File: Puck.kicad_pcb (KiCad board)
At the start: 2 copper layers, 40.1 x 33 mm, 15 parts, among them J1 TYPE-C-31-M-12, J2 AUTO_PROG_UART, U1 ESP32-C6-MINI-1-H4, U2 MCP9808T-E_MS, U4 AP2112K-3.3TRG1

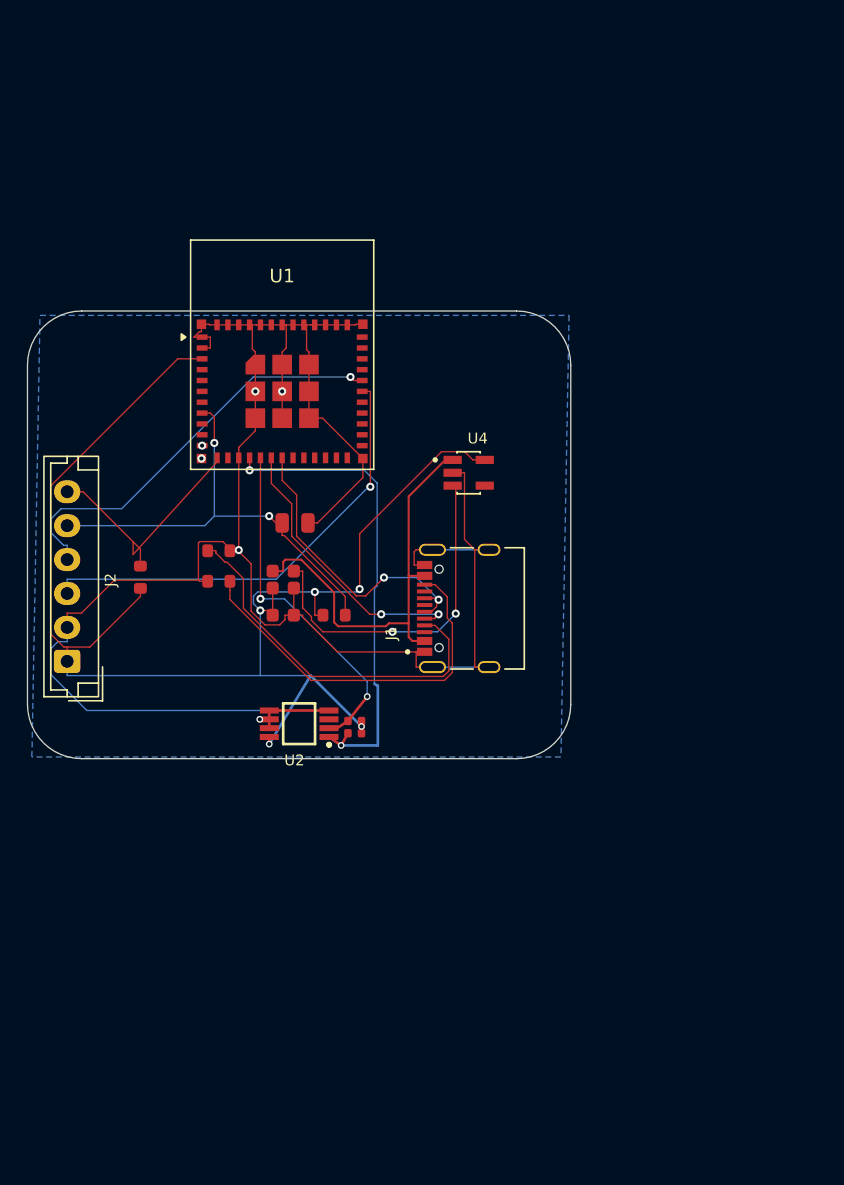
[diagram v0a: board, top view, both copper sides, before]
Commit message: Finished schematic + redid pcb layout
Original-author: Zachariah K. Sharma <zachariah.sharma@gmail.com>
Source-commit: d32a3a69c26190fe9d53ad46781c94031068a0a4
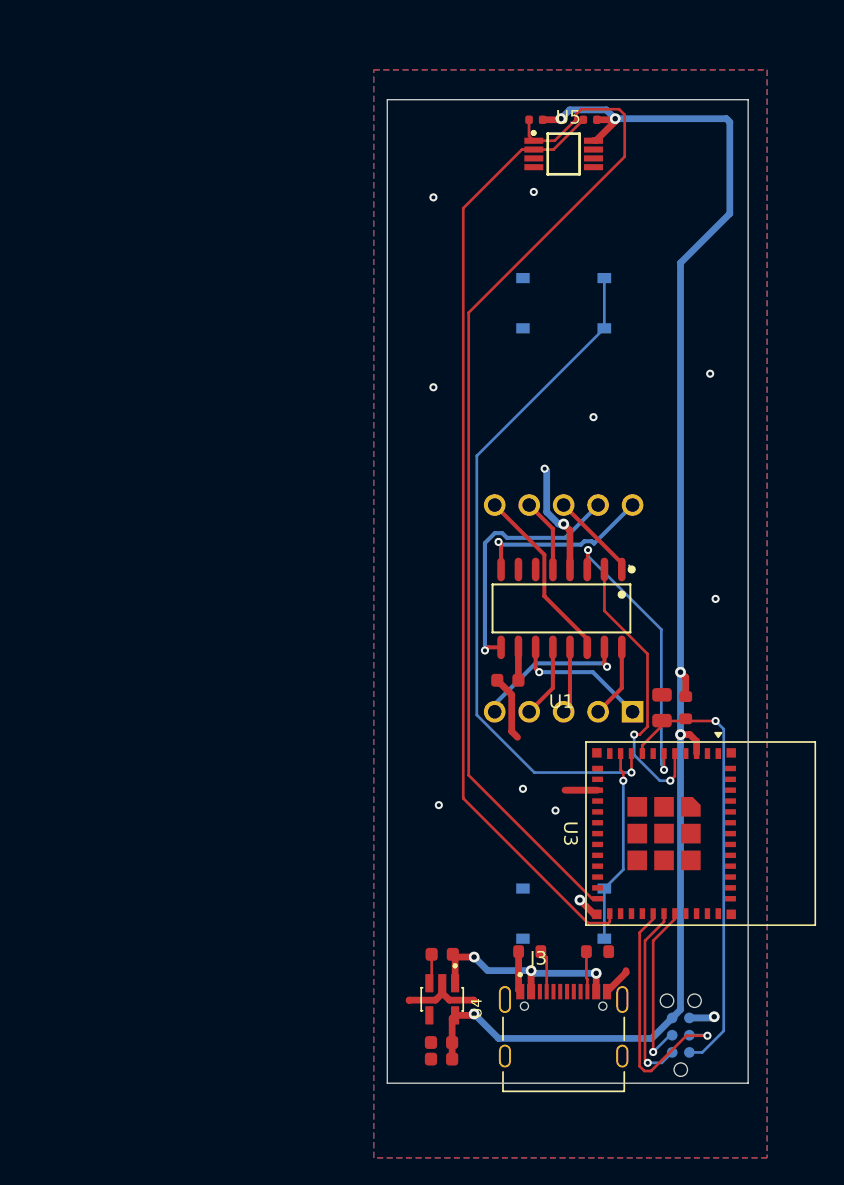
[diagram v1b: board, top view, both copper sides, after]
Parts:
- removed J1: TYPE-C-31-M-12, Footprints:HRO_TYPE-C-31-M-12
- removed J2: AUTO_PROG_UART, Connector_JST:JST_EH_B6B-EH-A_1x06_P2.50mm_Vertical
- removed R1, R2: 4.7kΩ, PCM_JLCPCB:R_0402
- removed R8: 10kΩ, PCM_JLCPCB:R_0603
- removed U2: MCP9808T-E_MS, Footprints:SOP65P490X110-8N
- added C1: 1 uF, PCM_JLCPCB:C_0603, F.Cu at (159.9, 101.8)
- added J3: TYPE-C-31-M-12, Footprints:HRO_TYPE-C-31-M-12, F.Cu at (164.0, 129.5)
- added J4: Conn_01x04_Socket, Connector:Tag-Connect_TC2030-IDC-NL_2x03_P1.27mm_Vertical, B.Cu at (172.6, 128.0)
- added LED1: SN760561W/16, easyeda2kicad:LED-SEG-TH_10P-L25.0-W19.0-P2.54-S15.2-BL, B.Cu at (164.0, 96.5)
- added R5: 5.1kΩ, PCM_JLCPCB:R_0603, F.Cu at (161.5, 121.8)
- added R6: 5.1kΩ, PCM_JLCPCB:R_0603, F.Cu at (166.5, 121.8)
- added SW1: SW_Push, Footprints:SW_TS-1187A-B-A-B_2term, B.Cu at (164.0, 74.0)
- added SW2: SW_Push, Footprints:SW_TS-1187A-B-A-B_2term, B.Cu at (164.0, 119.0)
- added U3: ESP32-C6-MINI-1, RF_Module:ESP32-C6-MINI-1, F.Cu at (171.4, 113.1)
- added U5: MCP9808T-E_MS, Footprints:SOP65P490X110-8N, F.Cu at (164.0, 63.0)
- R3, R4: value 5.1kΩ -> 4.7kΩ; footprint PCM_JLCPCB:R_0603 -> PCM_JLCPCB:R_0402
- U1: value ESP32-C6-MINI-1-H4 -> ET6226M; footprint Footprints:ESP32-C6-MINI-1 -> easyeda2kicad:SOP-16_L10.0-W3.9-P1.27-LS6.0-BL
- moved R3 41.9 mm to (165.9, 60.5), turned to 180 degrees
- moved R4 41.3 mm to (161.9, 60.5)
- moved U4 38.9 mm to (155.1, 125.3), turned to -90 degrees
- moved C4 35.5 mm to (155.0, 128.5), turned to 180 degrees
- moved C5 34.7 mm to (155.0, 129.7), turned to 180 degrees
- moved C3 30.6 mm to (155.1, 122.0), turned to 180 degrees
- moved C6 30.3 mm to (171.2, 103.8), turned to 90 degrees
- moved R7 26.8 mm to (173.0, 103.8), turned to -90 degrees
- moved U1 26.1 mm to (163.8, 96.5), turned to 180 degrees
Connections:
- C6 pad 1: EN -> /EN
- R3 pad 1: Net-(J1-CC1) -> +3.3V
- R3 pad 2: GND -> /IO19
- R4 pad 1: GND -> /IO18
- R4 pad 2: Net-(J1-CC2) -> +3.3V
- R7 pad 2: EN -> /EN
- U1 pad 1: GND -> /Seven Segment Display/DIG1
- U1 pad 10: (no net) -> +5V
- U1 pad 11: GND -> /Seven Segment Display/C
- U1 pad 12: IO0 -> /Seven Segment Display/D
- U1 pad 13: (no net) -> /Seven Segment Display/E
- U1 pad 14: GND -> /Seven Segment Display/F
- U1 pad 15: I2C_SDA -> /Seven Segment Display/G
- U1 pad 16: I2C_SCL -> /Seven Segment Display/DP
- U1 pad 2: GND -> /IO2
- U1 pad 3: +3.3V -> /IO3
- U1 pad 4: (no net) -> GND
- U1 pad 5: (no net) -> /Seven Segment Display/DIG2
- U1 pad 6: (no net) -> unconnected-(U1-GR3-Pad6)
- U1 pad 7: (no net) -> unconnected-(U1-GR4-Pad7)
- U1 pad 8: EN -> /Seven Segment Display/A
- U1 pad 9: (no net) -> /Seven Segment Display/B
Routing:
- net GND: track 158.9 -> 31.0 mm, vias 6 -> 13
- net /IO18: track 0.00 -> 76.5 mm
- net /IO19: track 0.00 -> 70.3 mm
- net /IO4: track 0.00 -> 50.7 mm, vias 0 -> 1
- net I2C_SDA: track 35.4 -> 0.00 mm, vias 2 -> 0
- net RXD0: track 33.9 -> 0.00 mm, vias 1 -> 0
- net EN: track 33.7 -> 0.00 mm, vias 2 -> 0
- net /EN: track 0.00 -> 33.0 mm, vias 0 -> 1
- net TXD0: track 31.1 -> 0.00 mm, vias 1 -> 0
- net Net-(J1-CC2): track 28.2 -> 0.00 mm
- net Net-(J1-CC1): track 27.7 -> 0.00 mm
- net I2C_SCL: track 26.0 -> 0.00 mm, vias 2 -> 0
- net Net-(U4-EN): track 25.6 -> 2.20 mm, vias 2 -> 0
- net USB_D+: track 22.4 -> 0.00 mm, vias 2 -> 0
- net /IO3: track 0.00 -> 21.3 mm, vias 0 -> 2
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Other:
- board size 40.1 x 33 mm -> 26.6 x 72.5 mm

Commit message: fix: Fix most design issues
Original-author: Ishan Karmakar <ishan.karmakar24@gmail.com>
Source-commit: a70ad4e322e6afcc76e9c4ecaab6da1a8e108794
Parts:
- removed U3: ESP32-C6-MINI-1, RF_Module:ESP32-C6-MINI-1
- added U2: ESP32-C6-MINI-1/U, PCM_Espressif:ESP32-C6-MINI-1, F.Cu at (174.1, 113.1)
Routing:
- net GND: track 31.0 -> 34.6 mm, vias 13 -> 16

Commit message: feat: Add revision to silkscreen
Original-author: Ishan Karmakar <ishan.karmakar24@gmail.com>
Source-commit: 2c4231b3e7d77dea71c8e7b3f19a2a28eaa9a6ca
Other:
- board text added: "${PROJECT_REV}"
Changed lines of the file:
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@@
 	)
 	(paper "A4")
+	(title_block
+		(title "Puck")
+		(date "2026-08-21")
+		(rev "${PROJECT_REV}")
+		(company "Vynte")
+	)
 	(layers
 		(0 "F.Cu" signal)
@@
 		(sheetname "/Type C Recepticle (No Flash)/")
 		(sheetfile "Type C Recepticle.kicad_sch")
+		(units
+			(unit
+				(name "A")
+				(pins "A5" "A6" "A7" "A8" "A4_B9" "B4_A9" "B8" "B7" "B6" "B5" "S1" "S2"
+					"S3" "S4" "A1_B12" "B1_A12"
+				)
+			)
+		)
 		(attr smd)
 		(duplicate_pad_numbers_are_jumpers no)
@@
 		(sheetname "/Temp Sensor/")
 		(sheetfile "Temp Sensor.kicad_sch")
+		(units
+			(unit
+				(name "A")
+				(pins "7" "6" "5" "2" "1" "8" "3" "4")
+			)
+		)
 		(attr smd)
 		(duplicate_pad_numbers_are_jumpers no)
@@
 		(layer "Edge.Cuts")
 	)
+	(gr_text "${PROJECT_REV}"
+		(at 154.75 76 90)
+		(layer "F.SilkS")
+		(effects
+			(font
+				(size 1.5 1.5)
+				(thickness 0.3)
+				(bold yes)
+			)
+			(justify left bottom)
+		)
+	)
 	(segment
